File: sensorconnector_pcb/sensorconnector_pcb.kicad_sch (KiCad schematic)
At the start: 4 parts, among them J1 RJ45_Shielded, J2 Conn_01x04_Male, J3 RJ45_Shielded

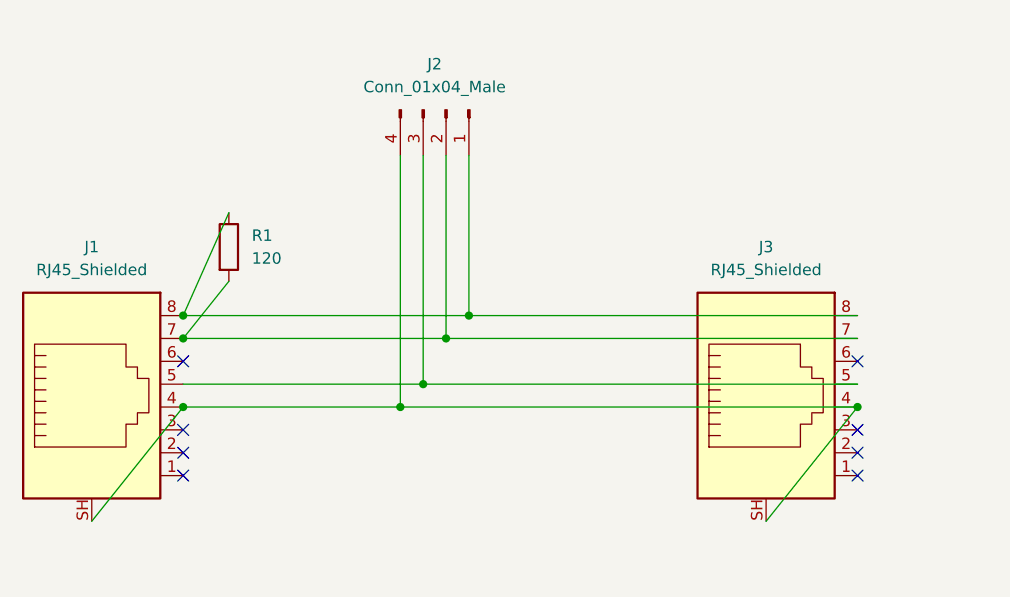
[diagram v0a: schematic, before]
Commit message: Updated to a multiplexed analog humidity sensor connector
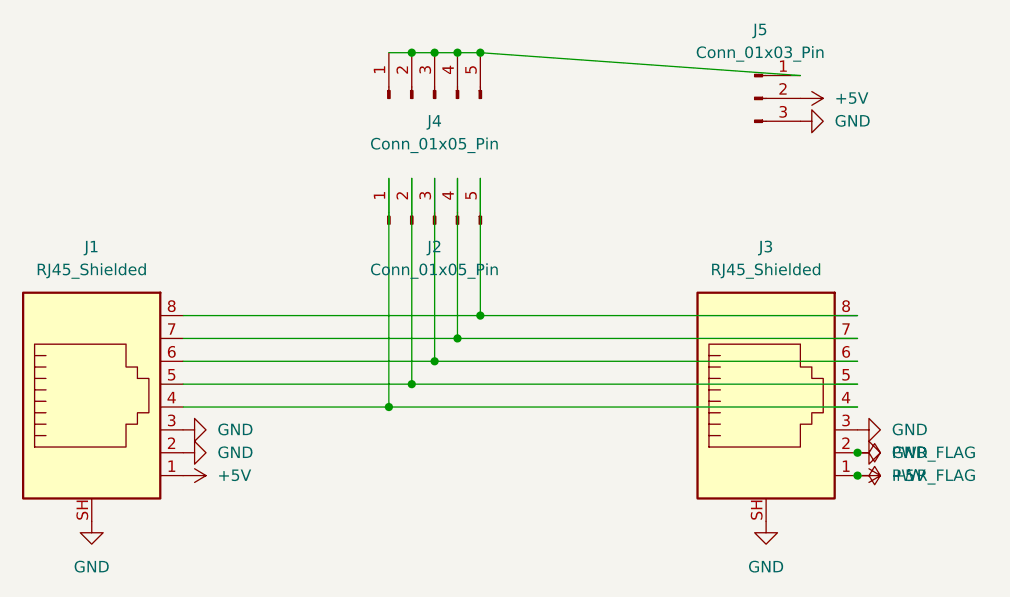
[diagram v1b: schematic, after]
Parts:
- removed J2: Conn_01x04_Male, TerminalBlock:TerminalBlock_bornier-4_P5.08mm, symbol Connector:Conn_01x04_Male
- removed R1: 120, Resistor_SMD:R_2010_5025Metric, symbol Device:R
- added J2, J4: Conn_01x05_Pin, Connector_PinHeader_2.54mm:PinHeader_1x05_P2.54mm_Vertical, symbol Connector:Conn_01x05_Pin
- added J5: Conn_01x03_Pin, TerminalBlock:TerminalBlock_bornier-3_P5.08mm, symbol Connector:Conn_01x03_Pin
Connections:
- net at J1.8, J3.8: now also J2.5 (Pin_5)
- net at J1.7, J3.7: now also J2.4 (Pin_4)
- net at J1.5, J3.5: now also J2.2 (Pin_2)
- net at J1.4, J3.4: now also J2.1 (Pin_1); no longer J1.SH, J3.SH
- net +5V: now reaches J1.1
- net +5V: now also J3.1, J5.2 (Pin_2)
- net GND: now reaches J1.2
- net GND: now also J1.3, J1.SH, J3.2, J3.3, J3.SH, J5.3 (Pin_3)
- net at J1.6: now also J3.6, J2.3 (Pin_3)
- new net: J4.1 (Pin_1), J4.2 (Pin_2), J4.3 (Pin_3), J4.4 (Pin_4), J4.5 (Pin_5), J5.1 (Pin_1)
- no-connect marks 8 -> 0
